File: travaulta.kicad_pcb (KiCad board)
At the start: 2 copper layers, 209.7 x 76.4 mm, 52 parts, among them J1 USB_C_Receptacle_USB2.0, Q1 2N7002, SW1 EC_SW, SW10 EC_SW, SW11 EC_SW, SW12 EC_SW, SW13 EC_SW, SW14 EC_SW, SW15 EC_SW, SW16 EC_SW, SW17 EC_SW, SW18 EC_SW, SW19 EC_SW, SW2 EC_SW, SW20 EC_SW, SW21 EC_SW, SW22 EC_SW, SW23 EC_SW, SW24 EC_SW, SW25 EC_SW, SW26 EC_SW, SW27 EC_SW, SW28 EC_SW, SW29 EC_SW, SW3 EC_SW, SW30 EC_SW, SW31 EC_SW, SW32 EC_SW, SW33 EC_SW, SW34 EC_SW, SW35 EC_SW, SW36 EC_SW, SW37 EC_SW, SW4 EC_SW, SW5 EC_SW, SW6 EC_SW, SW7 EC_SW, SW8 EC_SW, SW9 EC_SW, U1 STM32F411CCUx, U2 XC6206PxxxMR, Y1 16 MHz

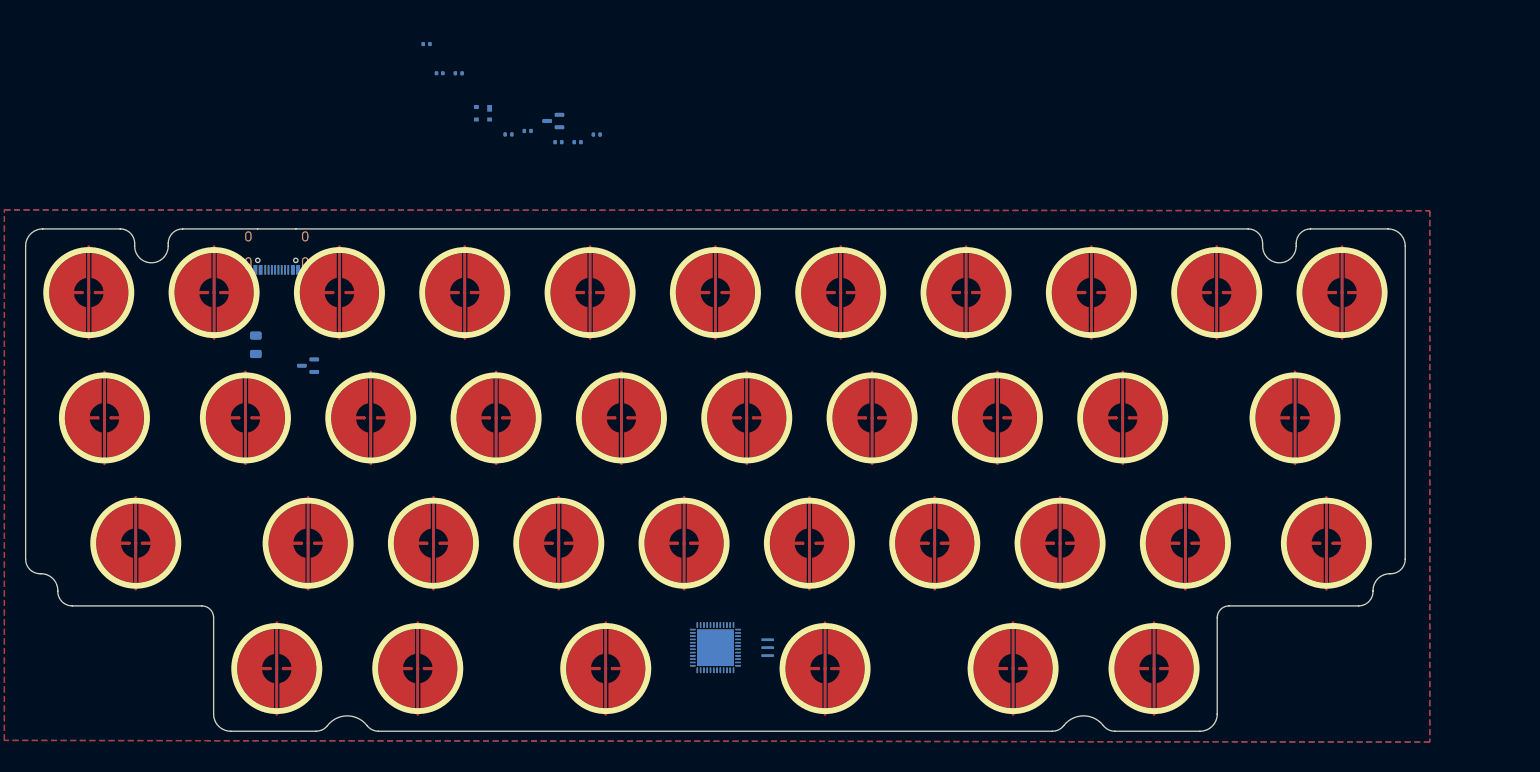
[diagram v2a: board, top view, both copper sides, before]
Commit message: analog schematics added
some questions
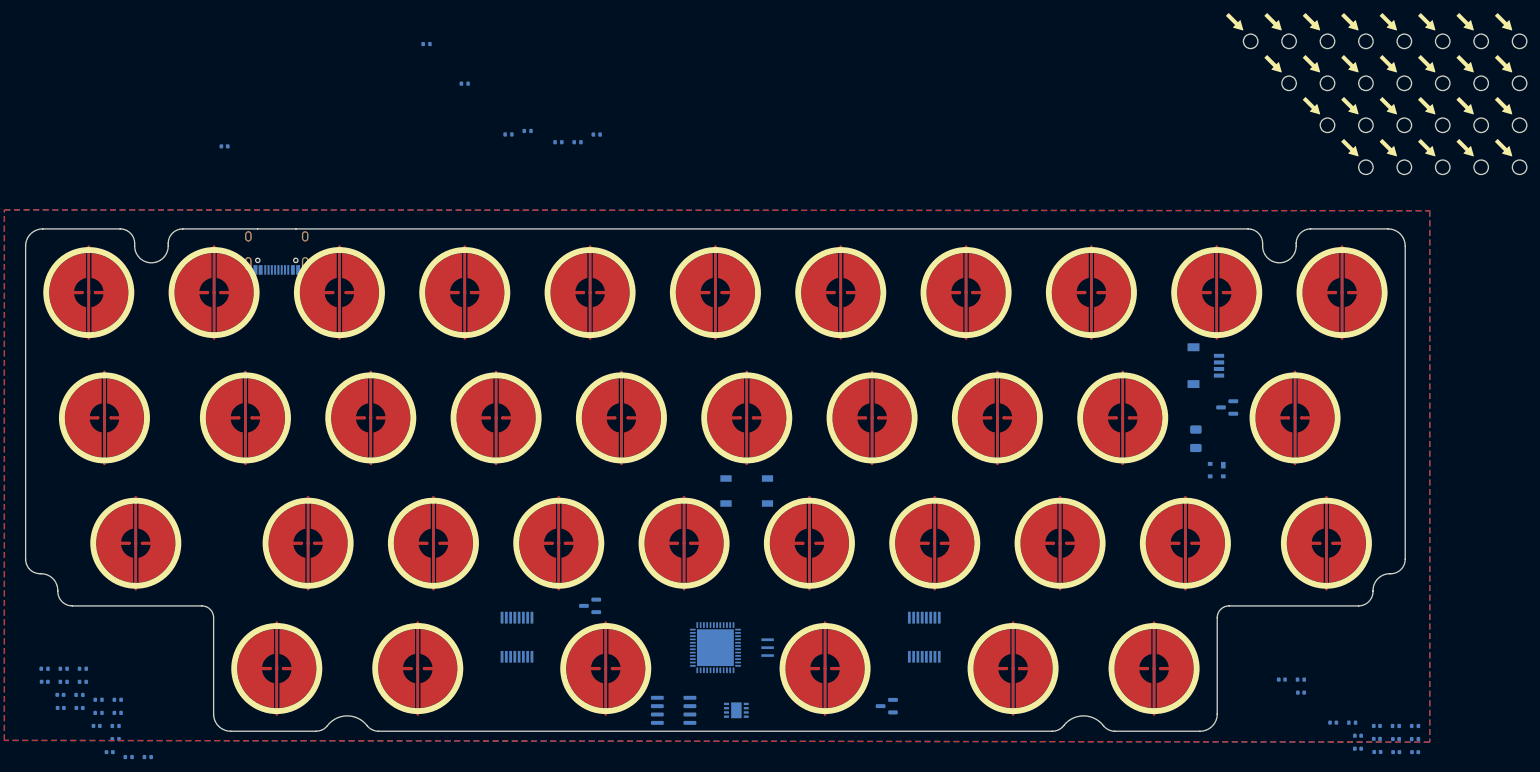
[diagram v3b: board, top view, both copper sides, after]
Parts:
- added C1: 4.7u, Capacitor_SMD:C_0402_1005Metric, B.Cu at (255.6, 127.0)
- added C10: 100n, Capacitor_SMD:C_0402_1005Metric, B.Cu at (249.8, 123.0)
- added C11: 1u, Capacitor_SMD:C_0402_1005Metric, B.Cu at (252.7, 125.0)
- added C12: 0.1u, Capacitor_SMD:C_0402_1005Metric, B.Cu at (47.3, 116.3)
- added C13: 0.1u, Capacitor_SMD:C_0402_1005Metric, B.Cu at (57.1, 127.0)
- added C14: 220p, Capacitor_SMD:C_0402_1005Metric, B.Cu at (55.2, 123.0)
- added C15: 0.1u, Capacitor_SMD:C_0402_1005Metric, B.Cu at (52.6, 120.3)
- added C16: 0.1u, Capacitor_SMD:C_0402_1005Metric, B.Cu at (49.7, 118.3)
- added C17: 1u, Capacitor_SMD:C_0402_1005Metric, B.Cu at (49.7, 120.3)
- added C2: 4.7u, Capacitor_SMD:C_0402_1005Metric, B.Cu at (246.9, 126.5)
- added C3: 1u, Capacitor_SMD:C_0402_1005Metric, B.Cu at (238.2, 118.0)
- added C4: 1u, Capacitor_SMD:C_0402_1005Metric, B.Cu at (252.7, 127.0)
- added C5: 1u, Capacitor_SMD:C_0402_1005Metric, B.Cu at (249.8, 125.0)
- added C6: 100n, Capacitor_SMD:C_0402_1005Metric, B.Cu at (235.3, 116.0)
- added C7: 100n, Capacitor_SMD:C_0402_1005Metric, B.Cu at (246.9, 124.5)
- added C8: 100n, Capacitor_SMD:C_0402_1005Metric, B.Cu at (243.1, 122.5)
- added C9: 100n, Capacitor_SMD:C_0402_1005Metric, B.Cu at (249.8, 127.0)
- added H1: MountingHole, cipulot_parts:HOLE_M2, B.Cu at (248.1, 31.7)
- added H10: MountingHole, cipulot_parts:HOLE_M2, B.Cu at (271.5, 25.3)
- added H11: MountingHole, cipulot_parts:HOLE_M2, B.Cu at (253.9, 25.3)
- added H12: MountingHole, cipulot_parts:HOLE_M2, B.Cu at (242.3, 19.0)
- added H13: MountingHole, cipulot_parts:HOLE_M2, B.Cu at (230.6, 19.0)
- added H14: MountingHole, cipulot_parts:HOLE_M2, B.Cu at (242.3, 31.7)
- added H15: MountingHole, cipulot_parts:HOLE_M2, B.Cu at (248.1, 38.1)
- added H16: MountingHole, cipulot_parts:HOLE_M2, B.Cu at (248.1, 19.0)
- added H17: MountingHole, cipulot_parts:HOLE_M2, B.Cu at (265.6, 25.3)
- added H18: MountingHole, cipulot_parts:HOLE_M2, B.Cu at (253.9, 19.0)
- added H19: MountingHole, cipulot_parts:HOLE_M2, B.Cu at (253.9, 31.7)
- added H2: MountingHole, cipulot_parts:HOLE_M2, B.Cu at (259.8, 19.0)
- added H20: MountingHole, cipulot_parts:HOLE_M2, B.Cu at (259.8, 31.7)
- added H21: MountingHole, cipulot_parts:HOLE_M2, B.Cu at (259.8, 25.3)
- added H22: MountingHole, cipulot_parts:HOLE_M2, B.Cu at (236.4, 19.0)
- added H23: MountingHole, cipulot_parts:HOLE_M2, B.Cu at (271.5, 38.1)
- added H24: MountingHole, cipulot_parts:HOLE_M2, B.Cu at (248.1, 25.3)
- added H25: MountingHole, cipulot_parts:HOLE_M2, B.Cu at (236.4, 25.3)
- added H26: MountingHole, cipulot_parts:HOLE_M2, B.Cu at (265.6, 19.0)
- added H3: MountingHole, cipulot_parts:HOLE_M2, B.Cu at (265.6, 31.7)
- added H4: MountingHole, cipulot_parts:HOLE_M2, B.Cu at (271.5, 19.0)
- added H5: MountingHole, cipulot_parts:HOLE_M2, B.Cu at (259.8, 38.1)
- added H6: MountingHole, cipulot_parts:HOLE_M2, B.Cu at (271.5, 31.7)
- added H7: MountingHole, cipulot_parts:HOLE_M2, B.Cu at (242.3, 25.3)
- added H8: MountingHole, cipulot_parts:HOLE_M2, B.Cu at (253.9, 38.1)
- added H9: MountingHole, cipulot_parts:HOLE_M2, B.Cu at (265.6, 38.1)
- added J2: JST, cipulot_parts:JST-SR-4, B.Cu at (223.8, 68.3)
- added Q2: 2N7002, Package_TO_SOT_SMD:SOT-23, B.Cu at (130.2, 104.8)
- added R10: 100k, Resistor_SMD:R_0402_1005Metric, B.Cu at (63.0, 127.8)
- added R11: 100k, Resistor_SMD:R_0402_1005Metric, B.Cu at (53.1, 116.3)
- added R12: 100k, Resistor_SMD:R_0402_1005Metric, B.Cu at (60.0, 127.8)
- added R13: 100k, Resistor_SMD:R_0402_1005Metric, B.Cu at (47.3, 114.3)
- added R14: 100k, Resistor_SMD:R_0402_1005Metric, B.Cu at (55.5, 119.0)
- added R15: 100k, Resistor_SMD:R_0402_1005Metric, B.Cu at (50.2, 114.3)
- added R16: 100k, Resistor_SMD:R_0402_1005Metric, B.Cu at (52.6, 118.3)
- added R17: 100k, Resistor_SMD:R_0402_1005Metric, B.Cu at (50.2, 116.3)
- added R18: 100k, Resistor_SMD:R_0402_1005Metric, B.Cu at (58.4, 119.0)
- added R19: 100k, Resistor_SMD:R_0402_1005Metric, B.Cu at (58.1, 125.0)
- added R20: 100k, Resistor_SMD:R_0402_1005Metric, B.Cu at (53.1, 114.3)
- added R21: 100, Resistor_SMD:R_0402_1005Metric, B.Cu at (55.5, 121.0)
- added R22: 100k, Resistor_SMD:R_0402_1005Metric, B.Cu at (58.4, 121.0)
- added R23: 1k, Resistor_SMD:R_0402_1005Metric, B.Cu at (58.1, 123.0)
- added R3: 10k, Resistor_SMD:R_0402_1005Metric, B.Cu at (255.6, 123.0)
- added R5: 100k, Resistor_SMD:R_0402_1005Metric, B.Cu at (246.0, 122.5)
- added R6: 10k, Resistor_SMD:R_0402_1005Metric, B.Cu at (252.7, 123.0)
- added R8: 100, Resistor_SMD:R_0402_1005Metric, B.Cu at (238.2, 116.0)
- added R9: 100, Resistor_SMD:R_0402_1005Metric, B.Cu at (255.6, 125.0)
- added SW38: SW_MEC_5G, cipulot_parts:SW_SPST_TL3342, B.Cu at (154.0, 87.3)
- added U3: 74HC4051, cipulot_parts:TSSOP16, B.Cu at (181.0, 109.5)
- added U4: 74HC4051, cipulot_parts:TSSOP16, B.Cu at (119.1, 109.5)
- added U5: OPA350, Package_SO:SOIC-8_3.9x4.9mm_P1.27mm, B.Cu at (142.9, 120.7)
- added U6: MAX5423, cipulot_parts:MAX5423, B.Cu at (152.4, 120.7)
- moved F_USBC1 143.6 mm to (222.2, 79.4)
- moved U2 139.8 mm to (227.0, 74.6)
- moved D1 124.0 mm to (225.4, 84.1)
- moved Q1 102.4 mm to (175.3, 120.0)
- moved C_USBSHIELD1 34.5 mm to (74.6, 34.9)
- moved R7 1.83 mm to (111.1, 25.4)
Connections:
- net SPI1_MSIO renamed SPI1_MISO
- R1 pad 1: unconnected-(R1-Pad1) -> Net-(U1-Pad39)
- R2 pad 1: ROW1 -> ROW3
- R2 pad 2: unconnected-(R2-Pad2) -> Net-(U1-Pad40)
- U1 pad 13: ADC -> RES_W
- U1 pad 38: unconnected-(U1-Pad38) -> Net-(U1-Pad38)
- U1 pad 39: unconnected-(U1-Pad39) -> Net-(U1-Pad39)
- U1 pad 40: unconnected-(U1-Pad40) -> Net-(U1-Pad40)

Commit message: autosave
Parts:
- moved R2 106.0 mm to (76.5, 130.7)
- moved R1 106.0 mm to (64.0, 117.0)
- moved R4 106.0 mm to (79.4, 130.2)
- moved R7 106.0 mm to (69.8, 123.0)
- moved R_USBSHIELD1 50.8 mm to (74.6, 31.8)
- moved R_USB2 44.2 mm to (84.1, 31.8)
- moved R_USB1 40.8 mm to (90.5, 30.2)
- moved J1 9.97 mm to (82.5, 39.7)
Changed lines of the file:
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@@
   )
   (footprint "Resistor_SMD:R_0402_1005Metric" (layer "B.Cu")
-    (at 111.125 25.4 180)
+    (at 69.817262 122.9925 180)
     (descr "Resistor SMD 0402 (1005 Metric), square (rectangular) end terminal, IPC_7351 nominal, (Body size source: IPC-SM-782 page 72, https://www.pcb-3d.com/wordpress/wp-content/uploads/ipc-sm-782a_amendment_1_and_2.pdf), generated with kicad-footprint-generator")
     (tags "resistor")
@@
   )
   (footprint "Resistor_SMD:R_0402_1005Metric" (layer "B.Cu")
-    (at 117.772738 33.1125 180)
+    (at 76.465 130.705 180)
     (descr "Resistor SMD 0402 (1005 Metric), square (rectangular) end terminal, IPC_7351 nominal, (Body size source: IPC-SM-782 page 72, https://www.pcb-3d.com/wordpress/wp-content/uploads/ipc-sm-782a_amendment_1_and_2.pdf), generated with kicad-footprint-generator")
     (tags "resistor")
@@
   )
   (footprint "Resistor_SMD:R_0402_1005Metric" (layer "B.Cu")
-    (at 120.682738 32.5825 180)
+    (at 79.375 130.175 180)
     (descr "Resistor SMD 0402 (1005 Metric), square (rectangular) end terminal, IPC_7351 nominal, (Body size source: IPC-SM-782 page 72, https://www.pcb-3d.com/wordpress/wp-content/uploads/ipc-sm-782a_amendment_1_and_2.pdf), generated with kicad-footprint-generator")
     (tags "resistor")
@@
   )
   (footprint "Resistor_SMD:R_0402_1005Metric" (layer "B.Cu")
-    (at 131.182738 33.1325 180)
+    (at 90.4875 30.1625 180)
     (descr "Resistor SMD 0402 (1005 Metric), square (rectangular) end terminal, IPC_7351 nominal, (Body size source: IPC-SM-782 page 72, https://www.pcb-3d.com/wordpress/wp-content/uploads/ipc-sm-782a_amendment_1_and_2.pdf), generated with kicad-footprint-generator")
     (tags "resistor")
@@
   )
   (footprint "Connector_USB:USB_C_Receptacle_HRO_TYPE-C-31-M-12" (layer "B.Cu")
-    (at 82.55 49.657)
+    (at 82.55 39.6875)
     (descr "USB Type-C receptacle for USB 2.0 and PD, http://www.krhro.com/uploads/soft/180320/1-1P320120243.pdf")
     (tags "usb usb-c 2.0 pd")
@@
   )
   (footprint "Resistor_SMD:R_0402_1005Metric" (layer "B.Cu")
-    (at 128.272738 34.2925 180)
+    (at 84.1375 31.75 180)
     (descr "Resistor SMD 0402 (1005 Metric), square (rectangular) end terminal, IPC_7351 nominal, (Body size source: IPC-SM-782 page 72, https://www.pcb-3d.com/wordpress/wp-content/uploads/ipc-sm-782a_amendment_1_and_2.pdf), generated with kicad-footprint-generator")
     (tags "resistor")
@@
   )
   (footprint "Resistor_SMD:R_0402_1005Metric" (layer "B.Cu")
-    (at 125.362738 34.2925 180)
+    (at 74.6125 31.75 180)
     (descr "Resistor SMD 0402 (1005 Metric), square (rectangular) end terminal, IPC_7351 nominal, (Body size source: IPC-SM-782 page 72, https://www.pcb-3d.com/wordpress/wp-content/uploads/ipc-sm-782a_amendment_1_and_2.pdf), generated with kicad-footprint-generator")
     (tags "resistor")
@@
   )
   (footprint "Resistor_SMD:R_0402_1005Metric" (layer "B.Cu")
-    (at 105.312738 19.3725 180)
+    (at 64.005 116.965 180)
     (descr "Resistor SMD 0402 (1005 Metric), square (rectangular) end terminal, IPC_7351 nominal, (Body size source: IPC-SM-782 page 72, https://www.pcb-3d.com/wordpress/wp-content/uploads/ipc-sm-782a_amendment_1_and_2.pdf), generated with kicad-footprint-generator")
     (tags "resistor")

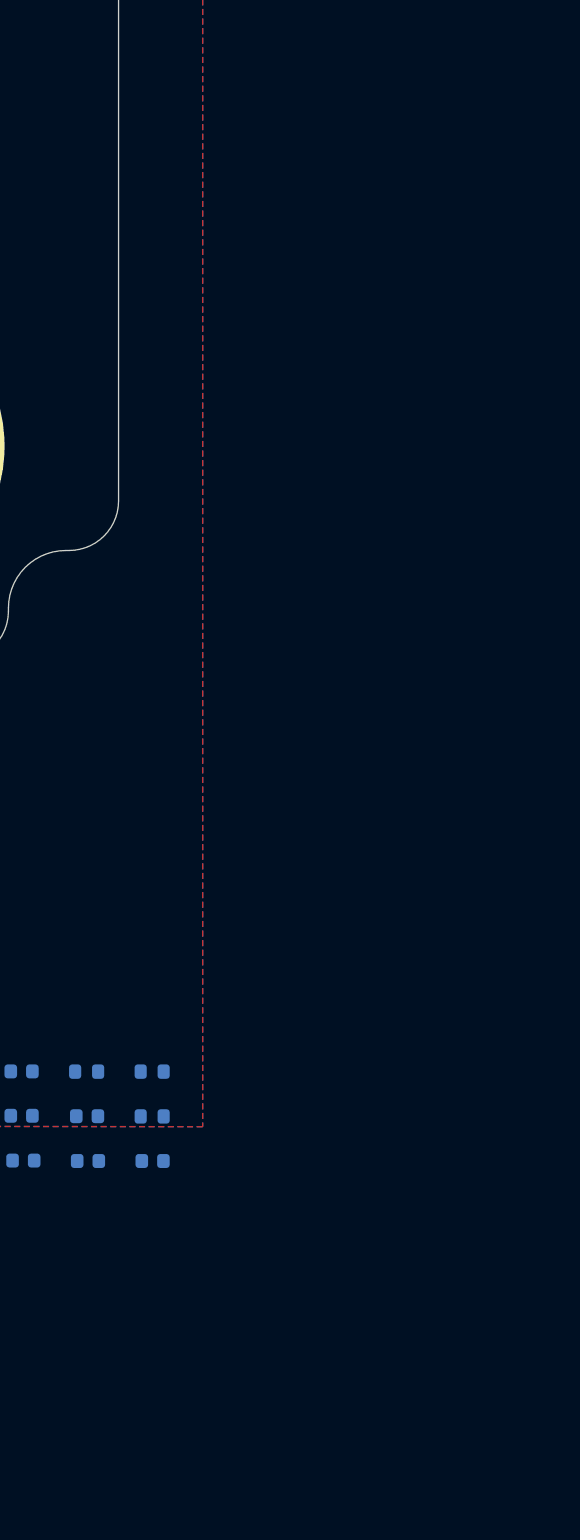
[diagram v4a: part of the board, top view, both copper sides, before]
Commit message: question marker
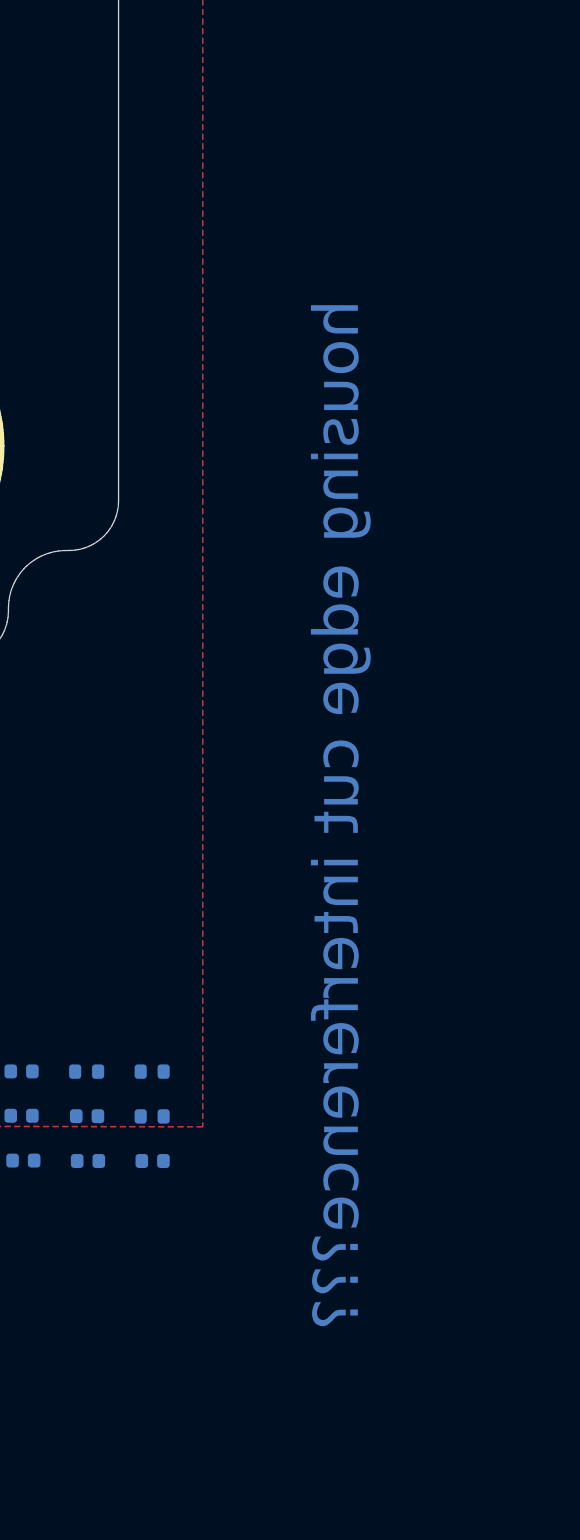
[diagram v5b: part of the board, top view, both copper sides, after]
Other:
- board text added: "housing edge cut interference???"
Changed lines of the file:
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@@
   (gr_line locked (start 51.466 104.774999) (end 71.150001 104.774999) (layer "Edge.Cuts") (width 0.05))
   (gr_arc locked (start 249.184374 102.433999) (mid 249.931233 100.630857) (end 251.734375 99.884) (layer "Edge.Cuts") (width 0.05))
+  (gr_text "housing edge cut interference???\n" (at 263.779 111.633 90) (layer "B.Cu")
+    (effects (font (size 2 2) (thickness 0.3)) (justify mirror))
+  )
   (zone (net 2) (net_name "GND") (layers F&B.Cu) (hatch edge 0.508)
     (connect_pads (clearance 0))
